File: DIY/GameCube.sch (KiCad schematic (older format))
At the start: 5 parts, among them P1 GC Ctrl slot, P2 GC Ctrl slot, P3 GC Ctrl slot, P4 GC Ctrl slot

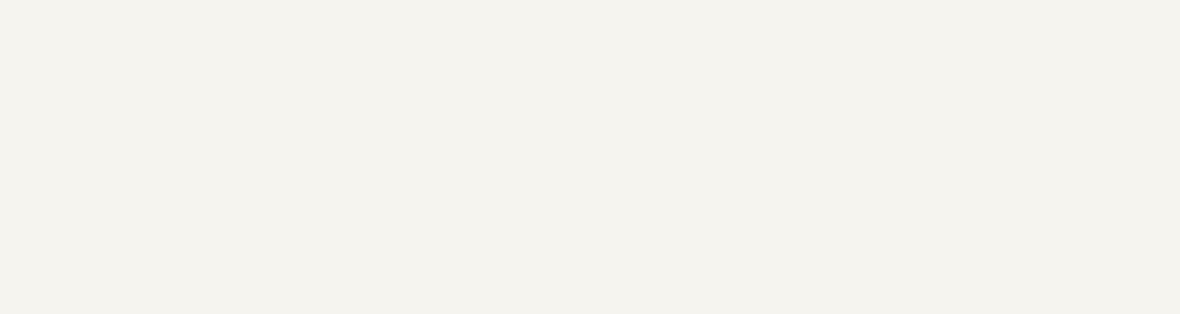
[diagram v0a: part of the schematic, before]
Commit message: [DIY] Add note to cable schematics to underline how important I39 is.
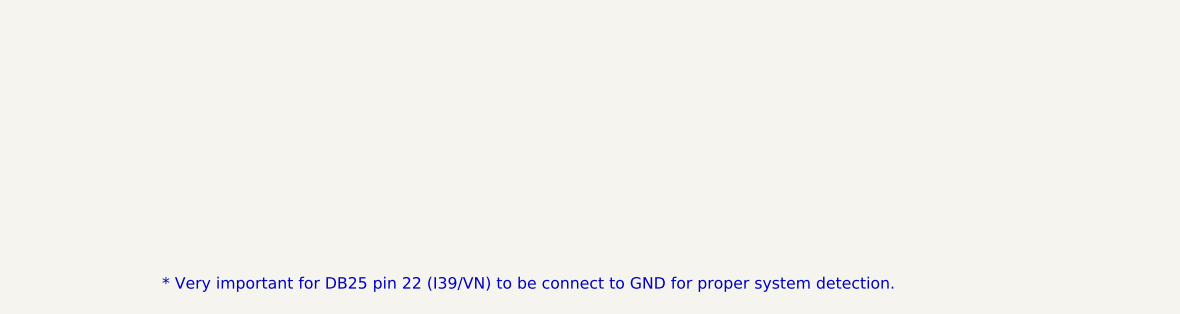
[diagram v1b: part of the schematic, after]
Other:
- note added: "* Very important for DB25 pin 22 (I39/VN) to be connect to GND for proper system detection."
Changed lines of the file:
@@
 Text Label 6500 5000 2    50   ~ 0
 IO27
+Text Notes 6350 6900 0    50   ~ 0
+* Very important for DB25 pin 22 (I39/VN) to be connect to GND for proper system detection.
 $EndSCHEMATC

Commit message: Use new port symbol in cable schematic
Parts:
- P1, P2, P3, P4: symbol Connector_Generic_Shielded:Conn_01x06_Shielded -> Connector_Gaming:GameCube
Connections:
- wire segments 70 -> 74
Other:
- note added: "Connectors facing console"

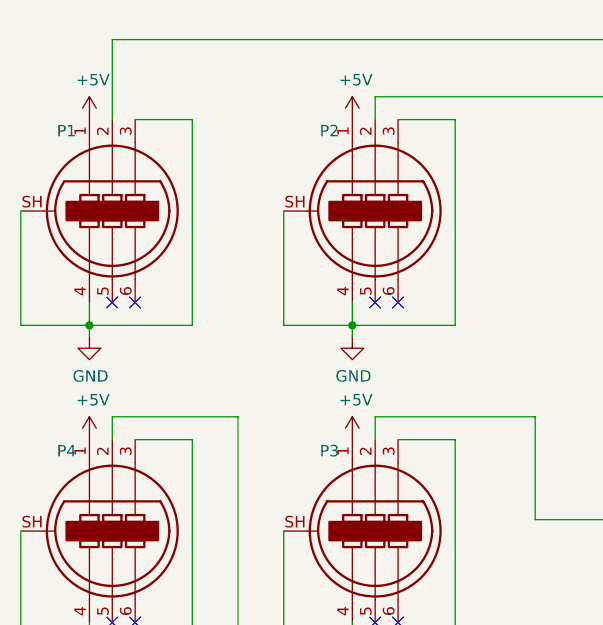
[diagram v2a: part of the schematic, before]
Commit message: Update adapter cable schematics
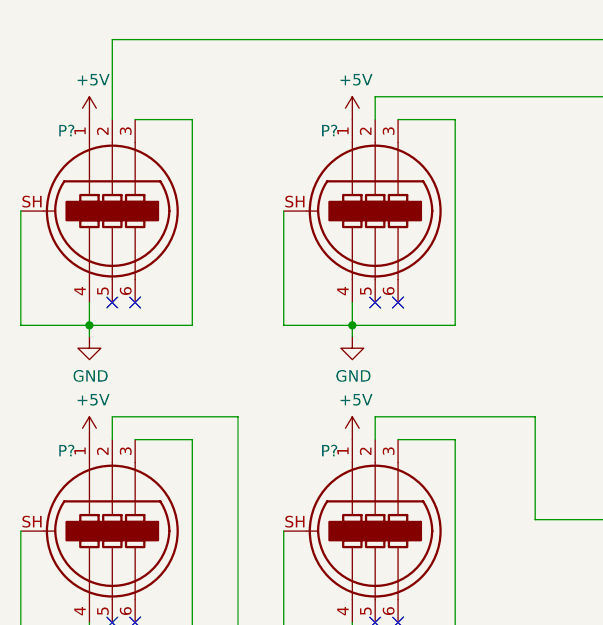
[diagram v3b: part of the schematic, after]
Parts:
- gave numbers to parts that had none: 1
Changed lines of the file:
@@
 $Descr USLetter 11000 8500
 encoding utf-8
-Sheet 6 7
+Sheet 6 10
 Title "BlueRetro - GameCube adapter cable"
 Date "2020-10-02"
@@
 P 6650 3950
 AR Path="/5F50506C" Ref="#PWR?"  Part="1"
-AR Path="/5F457D26/5F50506C" Ref="#PWR?"  Part="1"
+AR Path="/5F457D26/5F50506C" Ref="#PWR0110"  Part="1"
 F 0 "#PWR?" H 6650 3700 50  0001 C CNN
 F 1 "GND" H 6655 3777 50  0000 C CNN
@@
 P 6750 3750
 AR Path="/5F505079" Ref="#PWR?"  Part="1"
-AR Path="/5F457D26/5F505079" Ref="#PWR?"  Part="1"
+AR Path="/5F457D26/5F505079" Ref="#PWR0111"  Part="1"
 F 0 "#PWR?" H 6750 3600 50  0001 C CNN
 F 1 "+5V" H 6765 3923 50  0000 C CNN
@@
 AR Path="/5F505081" Ref="P?"  Part="1"
 AR Path="/5F457D26/5F505081" Ref="P1"  Part="1"
-F 0 "P1" V 4350 2150 50  0000 C CNN
+F 0 "P?" V 4350 2150 50  0000 C CNN
 F 1 "GC Ctrl slot" H 4522 3174 50  0001 C CNN
 F 2 "" H 4600 2850 50  0001 C CNN
@@
 AR Path="/5F505087" Ref="P?"  Part="1"
 AR Path="/5F457D26/5F505087" Ref="P2"  Part="1"
-F 0 "P2" V 5500 2150 50  0000 C CNN
+F 0 "P?" V 5500 2150 50  0000 C CNN
 F 1 "GC Ctrl slot" H 5672 3174 50  0001 C CNN
 F 2 "" H 5750 2850 50  0001 C CNN
@@
 AR Path="/5F50508D" Ref="P?"  Part="1"
 AR Path="/5F457D26/5F50508D" Ref="P3"  Part="1"
-F 0 "P3" V 5500 3550 50  0000 C CNN
+F 0 "P?" V 5500 3550 50  0000 C CNN
 F 1 "GC Ctrl slot" H 5672 4574 50  0001 C CNN
 F 2 "" H 5750 4250 50  0001 C CNN
@@
 AR Path="/5F505093" Ref="P?"  Part="1"
 AR Path="/5F457D26/5F505093" Ref="P4"  Part="1"
-F 0 "P4" V 4350 3550 50  0000 C CNN
+F 0 "P?" V 4350 3550 50  0000 C CNN
 F 1 "GC Ctrl slot" H 4522 4574 50  0001 C CNN
 F 2 "" H 4600 4250 50  0001 C CNN
@@
 P 5150 4900
 AR Path="/5F505099" Ref="#PWR?"  Part="1"
-AR Path="/5F457D26/5F505099" Ref="#PWR?"  Part="1"
+AR Path="/5F457D26/5F505099" Ref="#PWR0109"  Part="1"
 F 0 "#PWR?" H 5150 4650 50  0001 C CNN
 F 1 "GND" H 5155 4727 50  0000 C CNN
@@
 P 4000 4900
 AR Path="/5F50509F" Ref="#PWR?"  Part="1"
-AR Path="/5F457D26/5F50509F" Ref="#PWR?"  Part="1"
+AR Path="/5F457D26/5F50509F" Ref="#PWR0105"  Part="1"
 F 0 "#PWR?" H 4000 4650 50  0001 C CNN
 F 1 "GND" H 4005 4727 50  0000 C CNN
@@
 P 5150 3500
 AR Path="/5F5050A5" Ref="#PWR?"  Part="1"
-AR Path="/5F457D26/5F5050A5" Ref="#PWR?"  Part="1"
+AR Path="/5F457D26/5F5050A5" Ref="#PWR0107"  Part="1"
 F 0 "#PWR?" H 5150 3250 50  0001 C CNN
 F 1 "GND" H 5155 3327 50  0000 C CNN
@@
 P 4000 3500
 AR Path="/5F5050AB" Ref="#PWR?"  Part="1"
-AR Path="/5F457D26/5F5050AB" Ref="#PWR?"  Part="1"
+AR Path="/5F457D26/5F5050AB" Ref="#PWR0103"  Part="1"
 F 0 "#PWR?" H 4000 3250 50  0001 C CNN
 F 1 "GND" H 4005 3327 50  0000 C CNN
@@
 P 5150 2550
 AR Path="/5F5050B1" Ref="#PWR?"  Part="1"
-AR Path="/5F457D26/5F5050B1" Ref="#PWR?"  Part="1"
+AR Path="/5F457D26/5F5050B1" Ref="#PWR0106"  Part="1"
 F 0 "#PWR?" H 5150 2400 50  0001 C CNN
 F 1 "+5V" H 5165 2723 50  0000 C CNN
@@
 P 5150 3950
 AR Path="/5F5050B7" Ref="#PWR?"  Part="1"
-AR Path="/5F457D26/5F5050B7" Ref="#PWR?"  Part="1"
+AR Path="/5F457D26/5F5050B7" Ref="#PWR0108"  Part="1"
 F 0 "#PWR?" H 5150 3800 50  0001 C CNN
 F 1 "+5V" H 5165 4123 50  0000 C CNN
@@
 P 4000 3950
 AR Path="/5F5050BD" Ref="#PWR?"  Part="1"
-AR Path="/5F457D26/5F5050BD" Ref="#PWR?"  Part="1"
+AR Path="/5F457D26/5F5050BD" Ref="#PWR0104"  Part="1"
 F 0 "#PWR?" H 4000 3800 50  0001 C CNN
 F 1 "+5V" H 4015 4123 50  0000 C CNN
@@
 P 4000 2550
 AR Path="/5F5050C3" Ref="#PWR?"  Part="1"
-AR Path="/5F457D26/5F5050C3" Ref="#PWR?"  Part="1"
+AR Path="/5F457D26/5F5050C3" Ref="#PWR0102"  Part="1"
 F 0 "#PWR?" H 4000 2400 50  0001 C CNN
 F 1 "+5V" H 4015 2723 50  0000 C CNN
@@
 AR Path="/5F64B66F" Ref="J?"  Part="1"
 AR Path="/5F457716/5F64B66F" Ref="J?"  Part="1"
-AR Path="/5F457D26/5F64B66F" Ref="J?"  Part="1"
+AR Path="/5F457D26/5F64B66F" Ref="J8"  Part="1"
 F 0 "J?" H 7430 3846 50  0001 L CNN
 F 1 "DB25_Male" H 7050 2400 50  0000 L CNN
